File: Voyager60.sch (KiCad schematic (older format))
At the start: 231 parts, among them Q1 2N7002, SW1 6x6x5mm, U1 ATmega32U4, U2 PRTR5V0U2X, Y1 16Mhz

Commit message: Progress
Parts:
- USB1: footprint Type-C:HRO-TYPE-C-31-M-12 -> Type-C:HRO-TYPE-C-31-M-12-Assembly
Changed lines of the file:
@@
 F 0 "USB1" H 1075 9750 60  0000 C CNN
 F 1 "HRO-TYPE-C-31-M-12" V 875 9050 60  0000 C CNN
-F 2 "Type-C:HRO-TYPE-C-31-M-12" H 1275 9100 60  0001 C CNN
+F 2 "Type-C:HRO-TYPE-C-31-M-12-Assembly" H 1275 9100 60  0001 C CNN
 F 3 "" H 1275 9100 60  0001 C CNN
 	1    1275 9100

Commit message: Place components
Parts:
- removed U1: ATmega32U4, Housings_QFP:TQFP-44_10x10mm_Pitch0.8mm, symbol Voyager60-rescue:ATmega32U4
- added D44, D58, D62: SOD-123, Diodes_SMD:D_SOD-123, symbol Device:D_Small
- added K_SHIFT2: MX-1.25U, MX_Alps_Hybrid:MXOnly-1.25U, symbol MX_Alps_Hybrids:MX-1U
- added K_SHIFT3: MX-1U, MX_Alps_Hybrid:MXOnly-1U, symbol MX_Alps_Hybrids:MX-1U
- added K_SPACE3: MX-2.25U, MX_Alps_Hybrid:MXOnly-2.25U-ReversedStabilizers, symbol MX_Alps_Hybrids:MX-1U
- added K_SPACE4: MX-2.75U, MX_Alps_Hybrid:MXOnly-2.75U-ReversedStabilizers, symbol MX_Alps_Hybrids:MX-1U
- added K_SPACE5: MX-1.25U, MX_Alps_Hybrid:MXOnly-1.25U-FLIPPED, symbol MX_Alps_Hybrids:MX-1U
- added R44, R58, R62: 1k, Resistors_SMD:R_0805, symbol Device:R_Small
- added U1: ATmega32U4-MU, Housings_DFN_QFN:QFN-44-1EP_7x7mm_Pitch0.5mm, symbol MCU_Microchip_ATmega:ATmega32U4-MU
- C2, C3, C4, C5, C6, C7, C8: footprint Capacitors_SMD:C_0805 -> Capacitors_SMD:C_0603
- K_ALT2, K_RALT3: footprint MX_Alps_Hybrid:MXOnly-1.5U -> MX_Alps_Hybrid:MXOnly-1.5U-FLIPPED
- K_RALT2, K_RMENU2: footprint MX_Alps_Hybrid:MXOnly-1.25U -> MX_Alps_Hybrid:MXOnly-1.25U-FLIPPED
- K_RCTRL1, K_WIN2: footprint MX_Alps_Hybrid:MXOnly-1U -> MX_Alps_Hybrid:MXOnly-1U-FLIPPED
- K_RSHIFT1: footprint MX_Alps_Hybrid:MXOnly-2.75U -> MX_Alps_Hybrid:MXOnly-2.75U-FLIPPED
- SW1: value 6x6x5mm -> 5.2x5.2mm; footprint Molex-0548190589:PushButton_6x6mm_TH_Pretty -> Molex-0548190589:SKQG-1155865
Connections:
- net +5V: now also K_SHIFT3.3 (LED), K_SPACE3.3 (LED), K_SPACE4.3 (LED), U1.14 (VCC), U1.2 (UVCC), U1.24 (AVCC), U1.34 (VCC), U1.44 (AVCC), U1.7 (VBUS); no longer R70.1
- net COL0: now also U1.22 (PD5)
- net COL1: now also K_SHIFT3.1 (COL), U1.25 (PD4); no longer K_Z1.1 (COL)
- net COL10: now also K_.1.1 (COL), U1.37 (PF6); no longer K_/1.1 (COL)
- net COL11: now also K_/1.1 (COL), U1.38 (PF5); no longer K_RSHIFT1.1 (COL)
- net COL12: now also K_RSHIFT1.1 (COL), U1.39 (PF4)
- net COL13: now also U1.40 (PF1)
- net COL14: now also U1.41 (PF0)
- net COL2: now also K_Z1.1 (COL), U1.26 (PD6); no longer K_X1.1 (COL)
- net COL3: now also K_X1.1 (COL), K_SPACE3.1 (COL), U1.27 (PD7); no longer K_C1.1 (COL)
- net COL4: now also K_C1.1 (COL), U1.28 (PB4); no longer K_V1.1 (COL)
- net COL5: now also K_V1.1 (COL), U1.29 (PB5); no longer K_B1.1 (COL)
- net COL6: now also K_B1.1 (COL), U1.30 (PB6); no longer K_N1.1 (COL)
- net COL7: now also K_N1.1 (COL), K_SPACE4.1 (COL), U1.31 (PC6); no longer K_M1.1 (COL)
- net COL8: now also K_M1.1 (COL), U1.32 (PC7); no longer K_,1.1 (COL)
- net COL9: now also K_,1.1 (COL), U1.36 (PF7); no longer K_.1.1 (COL)
- net D+: now also U1.4 (D+)
- net D-: now also U1.3 (D-)
- net GND: now also U1.15 (GND), U1.23 (GND), U1.35 (GND), U1.43 (GND), U1.45 (GND), U1.5 (UGND)
- net LEDGND: now also R44.2, R58.2, R62.2
- net ROW0: now also U1.11 (PB3)
- net ROW1: now also U1.18 (PD0)
- net ROW2: now also U1.19 (PD1)
- net ROW3: now also D44.1 (K), U1.20 (PD2)
- net ROW4: now also D58.1 (K), D62.1 (K), U1.21 (PD3)
- net at R69.2: now also U1.12 (PB7)
- net at R70.2, SW1.2: now also U1.13 (~RESET)
- net at C8.1, Y1.3: now also U1.16 (XTAL2)
- net at C7.1, Y1.1: now also U1.17 (XTAL1)
- net at R71.2: now also U1.33 (~HWB~/PE2)
- net at C6.1: now also U1.6 (UCAP)
- net at R67.2, USB1.5 (DN2), USB1.7 (DN1): now also U2.3 (IO2); no longer U2.2 (IO1)
- net at R68.2, USB1.6 (DP1), USB1.8 (DP2): now also U2.2 (IO1); no longer U2.3 (IO2)
- new net: D44.2 (A), K_SHIFT3.2 (ROW)
- new net: K_SHIFT3.4 (LEDGND), R44.1
- new net: D58.2 (A), K_SPACE3.2 (ROW)
- new net: K_SPACE3.4 (LEDGND), R58.1
- new net: D62.2 (A), K_SPACE4.2 (ROW)
- new net: K_SPACE4.4 (LEDGND), R62.1
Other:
- moved on the sheet: C2, C3, C4, C5, C6, C7, C8, D46, D47, D48, D49, D50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

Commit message: Continue routing
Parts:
- removed D15: SOD-123, Diodes_SMD:D_SOD-123, symbol Device:D_Small
- removed K_EX1, K_RALT1, K_RMENU1, K_RWIN1, K_SRSHIFT4: MX-1U, MX_Alps_Hybrid:MXOnly-1U, symbol MX_Alps_Hybrids:MX-1U
- removed K_RCTRL1: MX-1U, MX_Alps_Hybrid:MXOnly-1U-FLIPPED, symbol MX_Alps_Hybrids:MX-1U
- removed K_SRSHIFT3: MX-1.75U, MX_Alps_Hybrid:MXOnly-1.75U, symbol MX_Alps_Hybrids:MX-1U
- removed R15: 1k, Resistors_SMD:R_0805, symbol Device:R_Small
- K_#1, K_#10, K_#2, K_#3, K_#4, K_#5, K_#6, K_#7, K_#8, K_#9, K_'1, K_,1, K_-1, K_.1, K_/1, K_;1, K_=1, K_A1, K_B1, K_C1, K_D1, K_E1, K_ESC1, K_F1, K_G1, K_H1, K_I1, K_J1, K_K1, K_L1, K_M1, K_N1, K_O1, K_P1, K_Q1, K_R1, K_RWIN3, K_S1, K_SBACK1, K_SBACK2, K_SHIFT3, K_SRSHIFT2, K_T1, K_U1, K_V1, K_W1, K_X1, K_Y1, K_Z1, K_[1, K_\2, K_]1: footprint MX_Alps_Hybrid:MXOnly-1U -> MX_Alps_Hybrid:MX-1U
- K_ALT1, K_CTRL1, K_RCTRL2, K_RWIN2, K_SHIFT2, K_WIN1: footprint MX_Alps_Hybrid:MXOnly-1.25U -> MX_Alps_Hybrid:MX-1.25U
- K_ALT2, K_CTRL2, K_RALT3: footprint MX_Alps_Hybrid:MXOnly-1.5U-FLIPPED -> MX_Alps_Hybrid:MX-1.5U-FLIPPED
- K_BACK1: footprint MX_Alps_Hybrid:MXOnly-2U -> MX_Alps_Hybrid:MX-2U
- K_CAPS1, K_SRSHIFT1: footprint MX_Alps_Hybrid:MXOnly-1.75U -> MX_Alps_Hybrid:MX-1.75U
- K_CAPS2, K_RALT2, K_RMENU2, K_SPACE5: footprint MX_Alps_Hybrid:MXOnly-1.25U-FLIPPED -> MX_Alps_Hybrid:MX-1.25U-FLIPPED
- K_ENTER1, K_SHIFT1: footprint MX_Alps_Hybrid:MXOnly-2.25U -> MX_Alps_Hybrid:MX-2.25U
- K_ENTER2: footprint MX_Alps_Hybrid:MXOnly-ISO-ROTATED-ReversedStabilizers -> MX_Alps_Hybrid:MX-ISO-ReversedStabilizers
- K_RCTRL3: footprint MX_Alps_Hybrid:MXOnly-1.5U -> MX_Alps_Hybrid:MX-1.5U-FLIPPED
- K_RSHIFT1: footprint MX_Alps_Hybrid:MXOnly-2.75U-FLIPPED -> MX_Alps_Hybrid:MX-2.75U-FLIPPED
- K_SPACE1: footprint MX_Alps_Hybrid:MXOnly-7U-ReversedStabilizers -> MX_Alps_Hybrid:MX-7U-ReversedStabilizers
- K_SPACE2: footprint MX_Alps_Hybrid:MXOnly-6.25U-ReversedStabilizers -> MX_Alps_Hybrid:MX-6.25U-ReversedStabilizers
- K_SPACE3: footprint MX_Alps_Hybrid:MXOnly-2.25U-ReversedStabilizers -> MX_Alps_Hybrid:MX-2.25U-ReversedStabilizers
- K_SPACE4: footprint MX_Alps_Hybrid:MXOnly-2.75U-ReversedStabilizers -> MX_Alps_Hybrid:MX-2.75U-ReversedStabilizers
- K_TAB1, K_\1: footprint MX_Alps_Hybrid:MXOnly-1.5U -> MX_Alps_Hybrid:MX-1.5U
- K_WIN2: footprint MX_Alps_Hybrid:MXOnly-1U-FLIPPED -> MX_Alps_Hybrid:MX-1U-FLIPPED
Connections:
- net +5V: now also K_ENTER2.3 (LED), K_RALT2.3 (LED), K_RALT3.3 (LED), K_RCTRL2.3 (LED), K_RCTRL3.3 (LED), K_RMENU2.3 (LED), K_RWIN2.3 (LED), K_RWIN3.3 (LED), K_SPACE5.3 (LED), K_SRSHIFT1.3 (LED), K_\2.3 (LED), R70.1
- net COL0: now also U1.38 (PF5); no longer U1.22 (PD5)
- net COL1: now also U1.36 (PF7); no longer U1.25 (PD4)
- net COL10: now also K_RALT2.1 (COL), U1.26 (PD6); no longer U1.37 (PF6)
- net COL11: now also K_RALT3.1 (COL), K_RWIN2.1 (COL), U1.25 (PD4); no longer U1.38 (PF5)
- net COL12: now also K_RMENU2.1 (COL), K_RWIN3.1 (COL), K_SRSHIFT1.1 (COL), U1.22 (PD5); no longer U1.39 (PF4)
- net COL13: now also K_ENTER2.1 (COL), K_RCTRL2.1 (COL), K_RCTRL3.1 (COL), K_\2.1 (COL), U1.21 (PD3); no longer U1.40 (PF1)
- net COL2: now also U1.37 (PF6); no longer U1.26 (PD6)
- net COL3: now also U1.39 (PF4); no longer K_SPACE3.1 (COL), U1.27 (PD7)
- net COL4: now also K_SPACE3.1 (COL), U1.32 (PC7); no longer U1.28 (PB4)
- net COL5: now also U1.31 (PC6); no longer K_SPACE1.1 (COL), K_SPACE2.2 (ROW), U1.29 (PB5)
- net COL6: now also K_SPACE1.1 (COL), K_SPACE2.1 (COL), K_SPACE5.2 (ROW)
- net COL7: now also U1.29 (PB5); no longer K_SPACE4.1 (COL), U1.31 (PC6)
- net COL8: now also K_SPACE4.1 (COL), U1.28 (PB4); no longer U1.32 (PC7)
- net COL9: now also U1.27 (PD7); no longer U1.36 (PF7)
- net ROW0: now also U1.9 (PB1); no longer U1.11 (PB3)
- net ROW1: now also U1.10 (PB2); no longer U1.18 (PD0)
- net ROW2: now also U1.11 (PB3); no longer U1.19 (PD1)
- net ROW3: now also U1.19 (PD1); no longer U1.20 (PD2)
- net ROW4: now also U1.20 (PD2); no longer U1.21 (PD3)
- net at D29.2 (A), K_\1.2 (ROW): now also K_\2.2 (ROW)
- net at K_\1.4 (LEDGND), R29.1: now also K_\2.4 (LEDGND)
- net at D43.2 (A), K_ENTER1.2 (ROW): now also K_ENTER2.2 (ROW)
- net at K_ENTER1.4 (LEDGND), R43.1: now also K_ENTER2.4 (LEDGND)
- net at D56.2 (A), K_RSHIFT1.2 (ROW): now also K_SRSHIFT1.2 (ROW)
- net at K_RSHIFT1.4 (LEDGND), R56.1: now also K_SRSHIFT1.4 (LEDGND)
- net at D61.2 (A), K_SPACE1.2 (ROW): now also K_SPACE2.2 (ROW), K_SPACE5.1 (COL); no longer K_SPACE2.1 (COL)
- net at K_SPACE1.4 (LEDGND), K_SPACE2.4 (LEDGND), R61.1: now also K_SPACE5.4 (LEDGND)
- net at D63.2 (A): now also K_RALT2.2 (ROW)
- net at R63.1: now also K_RALT2.4 (LEDGND)
- net at D64.2 (A): now also K_RALT3.2 (ROW), K_RWIN2.2 (ROW)
- net at R64.1: now also K_RALT3.4 (LEDGND), K_RWIN2.4 (LEDGND)
- net at D65.2 (A): now also K_RCTRL2.2 (ROW), K_RCTRL3.2 (ROW)
- net at R65.1: now also K_RCTRL2.4 (LEDGND), K_RCTRL3.4 (LEDGND)
- net at D30.2 (A): now also K_RMENU2.2 (ROW), K_RWIN3.2 (ROW)
- net at R30.1: now also K_RMENU2.4 (LEDGND), K_RWIN3.4 (LEDGND)
- net COL14: no longer names the net of U1.41 (PF0)
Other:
- moved on the sheet: D58, D61, D62, K_RALT2, K_RALT3, K_RCTRL2, K_RCTRL3, K_RMENU2, K_RWIN2, K_RWIN3, K_SPACE1, K_SPACE2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

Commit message: Continue routing
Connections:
- net +5V: now also K_SHIFT2.3 (LED)
- net COL0: now also K_SHIFT2.1 (COL)
- net COL1: now also K_WIN2.1 (COL); no longer K_WIN2.2 (ROW)
- net at D45.2 (A), K_SHIFT1.2 (ROW): now also K_SHIFT2.2 (ROW)
- net at K_SHIFT1.4 (LEDGND), R45.1: now also K_SHIFT2.4 (LEDGND)
- net at D60.2 (A), K_WIN1.2 (ROW): now also K_WIN2.2 (ROW); no longer K_WIN2.1 (COL)
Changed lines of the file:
@@
 	1325 4075 1325 4700
-Wire Wire Line
-	2075 4550 2075 4375
-Wire Wire Line
-	2075 4375 1875 4375
-Wire Wire Line
-	1875 4375 1875 4125
-Wire Wire Line
-	1875 4750 1700 4750
-Wire Wire Line
-	1700 4750 1700 3925
-Wire Wire Line
-	1700 3925 2075 3925
 Wire Wire Line
 	2125 4600 2025 4600
@@
 	9475 3150 9475 3475
 Connection ~ 8475 3475
+Wire Wire Line
+	2075 3925 2075 4550
+Connection ~ 2075 3925
+Wire Wire Line
+	1875 4750 1875 4125
+Connection ~ 1875 4125
+Wire Wire Line
+	1475 3275 925  3275
+Wire Wire Line
+	725  3475 1200 3475
+Connection ~ 1200 3475
+Wire Wire Line
+	1325 3425 775  3425
+Connection ~ 1325 3425
+Wire Wire Line
+	875  3325 1425 3325
+Connection ~ 1425 3325
 $EndSCHEMATC

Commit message: Progress
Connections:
- net COL0: now also U1.39 (PF4); no longer U1.38 (PF5)
- net COL2: now also U1.38 (PF5); no longer U1.37 (PF6)
- net COL3: now also U1.37 (PF6); no longer U1.39 (PF4)
- net ROW3: now also U1.41 (PF0); no longer U1.19 (PD1)
- net ROW4: now also U1.40 (PF1); no longer U1.20 (PD2)
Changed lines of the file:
@@
 Text GLabel 8750 7300 2    60   Input ~ 0
 COL4
-Text GLabel 8750 8900 2    60   Input ~ 0
+Text GLabel 8750 9100 2    60   Input ~ 0
 COL3
-Text GLabel 8750 9100 2    60   Input ~ 0
+Text GLabel 8750 9000 2    60   Input ~ 0
 COL2
 Text GLabel 8750 9200 2    60   Input ~ 0
 COL1
-Text GLabel 8750 9000 2    60   Input ~ 0
+Text GLabel 8750 8900 2    60   Input ~ 0
 COL0
-Text GLabel 8750 7700 2    60   Input ~ 0
+Text GLabel 8750 8800 2    60   Input ~ 0
 ROW4
-Text GLabel 8750 7600 2    60   Input ~ 0
+Text GLabel 8750 8700 2    60   Input ~ 0
 ROW3
 Text GLabel 8750 6600 2    60   Input ~ 0

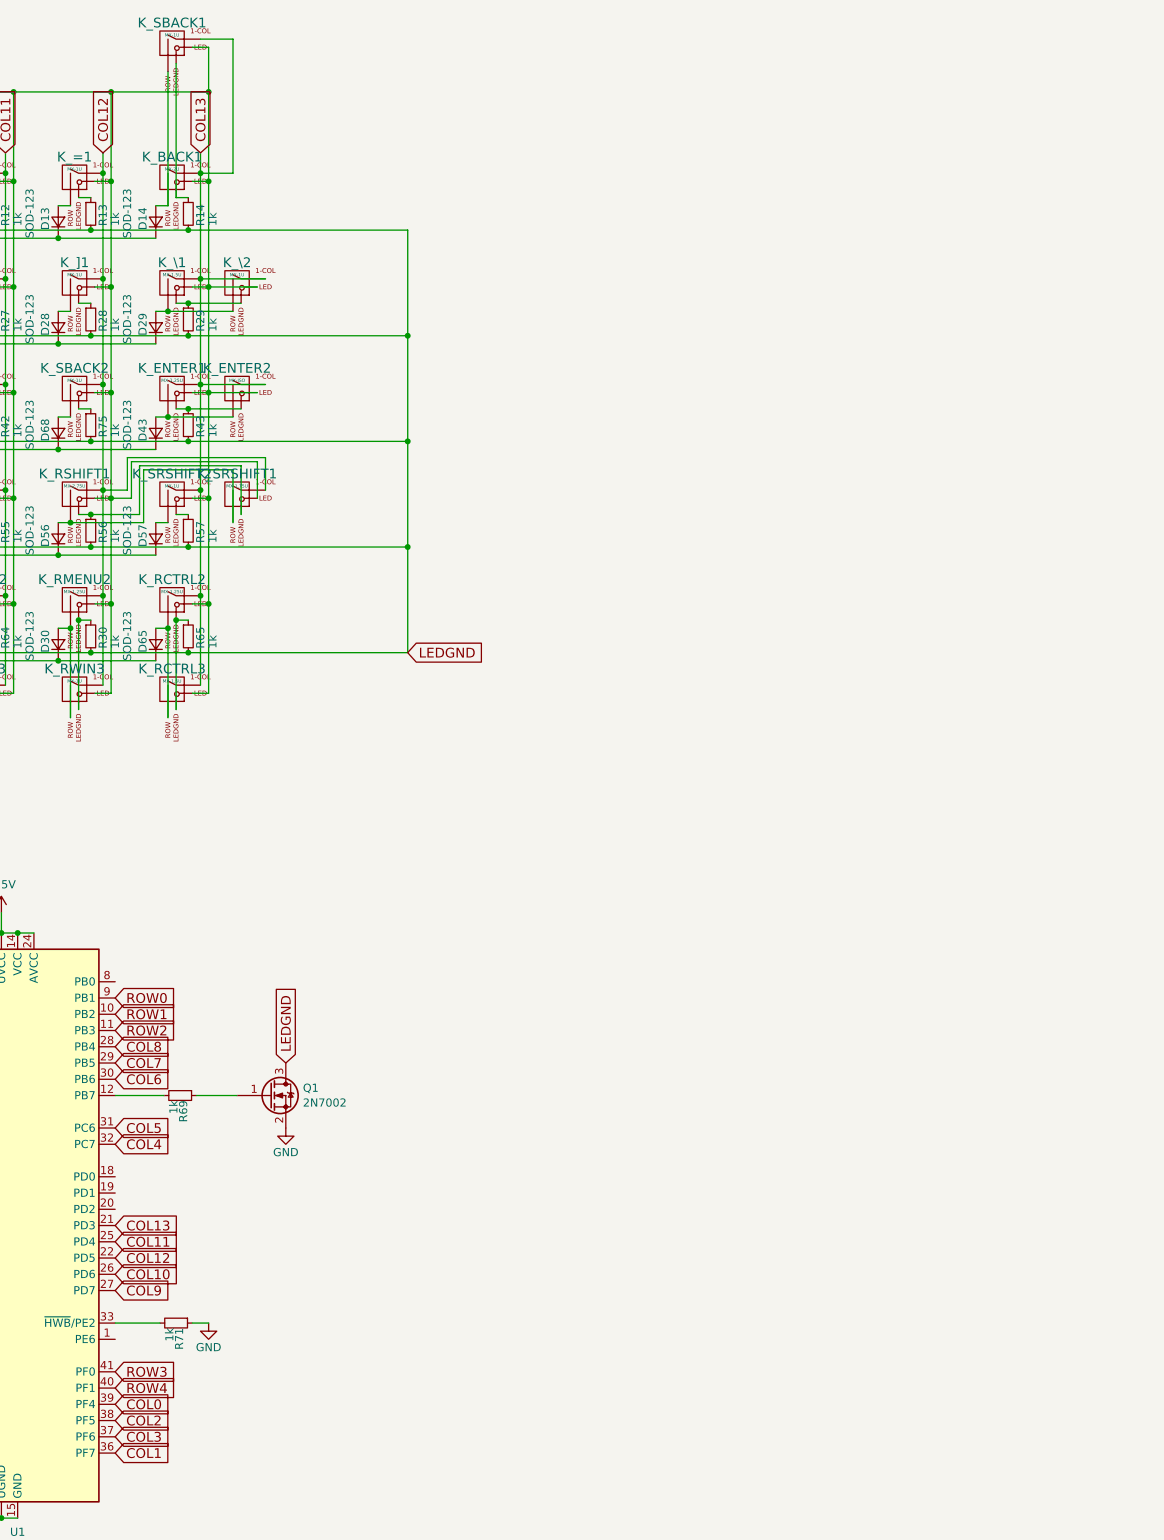
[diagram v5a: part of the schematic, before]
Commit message: Route RGBs
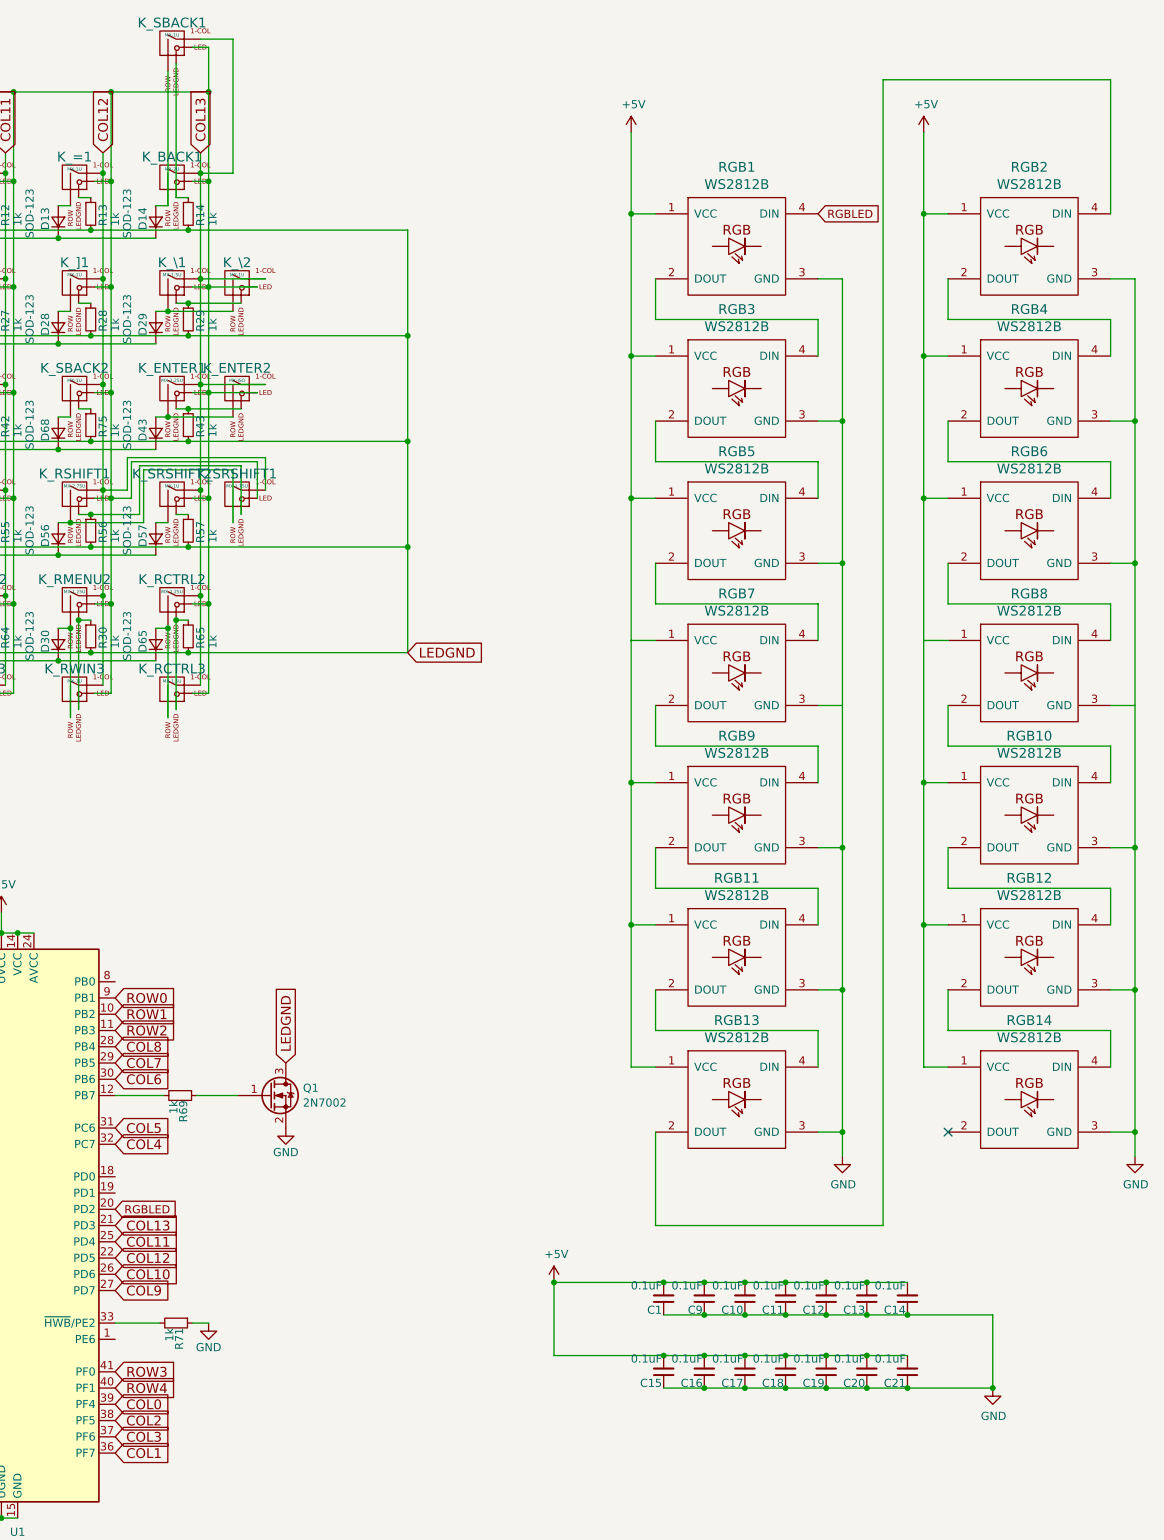
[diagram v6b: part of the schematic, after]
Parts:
- added C1, C10, C11, C12, C13, C14, C15, C16, C17, C18, C19, C20, C21, C9: 0.1uF, Capacitors_SMD:C_0603, symbol Device:C_Small
- added RGB1, RGB10, RGB11, RGB12, RGB13, RGB14, RGB2, RGB3, RGB4, RGB5, RGB6, RGB7, RGB8, RGB9: WS2812B, WS2812B:WS2812B, symbol ws2812b:WS2812B
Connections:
- net +5V: now also C1.2, C10.2, C11.2, C12.2, C13.2, C14.2, C15.2, C16.2, C17.2, C18.2, C19.2, C20.2, C21.2, C9.2, RGB1.1 (VCC), RGB10.1 (VCC), RGB11.1 (VCC), RGB12.1 (VCC), RGB13.1 (VCC), RGB14.1 (VCC), RGB2.1 (VCC), RGB3.1 (VCC), RGB4.1 (VCC), RGB5.1 (VCC), RGB6.1 (VCC), RGB7.1 (VCC), RGB8.1 (VCC), RGB9.1 (VCC)
- net GND: now also C1.1, C10.1, C11.1, C12.1, C13.1, C14.1, C15.1, C16.1, C17.1, C18.1, C19.1, C20.1, C21.1, C9.1, RGB1.3 (GND), RGB10.3 (GND), RGB11.3 (GND), RGB12.3 (GND), RGB13.3 (GND), RGB14.3 (GND), RGB2.3 (GND), RGB3.3 (GND), RGB4.3 (GND), RGB5.3 (GND), RGB6.3 (GND), RGB7.3 (GND), RGB8.3 (GND), RGB9.3 (GND)
- net RGBLED: now reaches U1.20 (PD2)
- net RGBLED: now also RGB1.4 (DIN)
- new net: RGB1.2 (DOUT), RGB3.4 (DIN)
- new net: RGB3.2 (DOUT), RGB5.4 (DIN)
- new net: RGB5.2 (DOUT), RGB7.4 (DIN)
- new net: RGB7.2 (DOUT), RGB9.4 (DIN)
- new net: RGB11.4 (DIN), RGB9.2 (DOUT)
- new net: RGB11.2 (DOUT), RGB13.4 (DIN)
- new net: RGB13.2 (DOUT), RGB2.4 (DIN)
- new net: RGB2.2 (DOUT), RGB4.4 (DIN)
- new net: RGB4.2 (DOUT), RGB6.4 (DIN)
- new net: RGB6.2 (DOUT), RGB8.4 (DIN)
- new net: RGB10.4 (DIN), RGB8.2 (DOUT)
- new net: RGB10.2 (DOUT), RGB12.4 (DIN)
- new net: RGB12.2 (DOUT), RGB14.4 (DIN)
- no-connect marks 1 -> 2

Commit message: Make alps variant
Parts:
- removed Q1: 2N7002, TO_SOT_Packages_SMD:SOT-23, symbol Transistor_FET:2N7002
- removed R1, R10, R11, R12, R13, R14, R16, R17, R18, R19, R2, R20, R21, R22, R23, R24, R25, R26, R27, R28, R29, R3, R30, R31, R32, R33, R34, R35, R36, R37, R38, R39, R4, R40, R41, R42, R43, R44, R45, R46, R47, R48, R49, R5, R50, R51, R52, R53, R54, R55, R56, R57, R58, R59, R6, R60, R61, R62, R63, R64, R65, R69, R7, R72, R75, R8, R9: 1k, Resistors_SMD:R_0805, symbol Device:R_Small
- added K_ALT3, K_CAPS3, K_RALT1: MX-1.5U, MX_Alps_Hybrid:ALPS-1.5U, symbol MX_Alps_Hybrids:MX-1U
- added K_ENTER3, K_ENTER4, K_ESC2: MX-1U, MX_Alps_Hybrid:ALPS-1U, symbol MX_Alps_Hybrids:MX-1U
- added K_RWIN1, K_WIN3: MX-1.25U, MX_Alps_Hybrid:ALPS-1.25U, symbol MX_Alps_Hybrids:MX-1U
- K_#1, K_#10, K_#2, K_#3, K_#4, K_#5, K_#6, K_#7, K_#8, K_#9, K_'1, K_,1, K_-1, K_.1, K_/1, K_;1, K_=1, K_A1, K_B1, K_C1, K_D1, K_E1, K_ESC1, K_F1, K_G1, K_H1, K_I1, K_J1, K_K1, K_L1, K_M1, K_N1, K_O1, K_P1, K_Q1, K_R1, K_RWIN3, K_S1, K_SBACK1, K_SBACK2, K_SHIFT3, K_SRSHIFT2, K_T1, K_U1, K_V1, K_W1, K_X1, K_Y1, K_Z1, K_[1, K_\2, K_]1: footprint MX_Alps_Hybrid:MX-1U -> MX_Alps_Hybrid:ALPS-1U
- K_ALT1, K_CTRL1, K_RCTRL2, K_RWIN2, K_SHIFT2, K_WIN1: footprint MX_Alps_Hybrid:MX-1.25U -> MX_Alps_Hybrid:ALPS-1.25U
- K_ALT2, K_CTRL2, K_RALT3, K_RCTRL3: footprint MX_Alps_Hybrid:MX-1.5U-FLIPPED -> MX_Alps_Hybrid:ALPS-1.5U
- K_BACK1: footprint MX_Alps_Hybrid:MX-2U -> MX_Alps_Hybrid:ALPS-2U
- K_CAPS1, K_SRSHIFT1: footprint MX_Alps_Hybrid:MX-1.75U -> MX_Alps_Hybrid:ALPS-1.75U
- K_CAPS2, K_RALT2, K_RMENU2, K_SPACE5: footprint MX_Alps_Hybrid:MX-1.25U-FLIPPED -> MX_Alps_Hybrid:ALPS-1.25U
- K_ENTER1, K_SHIFT1: footprint MX_Alps_Hybrid:MX-2.25U -> MX_Alps_Hybrid:ALPS-2.25U
- K_ENTER2: value MX-ISO -> MX-1U; footprint MX_Alps_Hybrid:MX-ISO-ReversedStabilizers -> MX_Alps_Hybrid:ALPS-1U
- K_RSHIFT1: footprint MX_Alps_Hybrid:MX-2.75U-FLIPPED -> MX_Alps_Hybrid:ALPS-2.75U
- K_SPACE1: footprint MX_Alps_Hybrid:MX-7U-ReversedStabilizers -> MX_Alps_Hybrid:ALPS-7U
- K_SPACE2: footprint MX_Alps_Hybrid:MX-6.25U-ReversedStabilizers -> MX_Alps_Hybrid:ALPS-6.25U
- K_SPACE3: footprint MX_Alps_Hybrid:MX-2.25U-ReversedStabilizers -> MX_Alps_Hybrid:ALPS-2.25U
- K_SPACE4: footprint MX_Alps_Hybrid:MX-2.75U-ReversedStabilizers -> MX_Alps_Hybrid:ALPS-2.75U
- K_TAB1, K_\1: footprint MX_Alps_Hybrid:MX-1.5U -> MX_Alps_Hybrid:ALPS-1.5U
- K_WIN2: footprint MX_Alps_Hybrid:MX-1U-FLIPPED -> MX_Alps_Hybrid:ALPS-1U
- U1: symbol MCU_Microchip_ATmega:ATmega32U4-MU -> Voyager60-rescue:ATmega32U4-MU-MCU_Microchip_ATmega
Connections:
- net labels removed: LEDGND
- wire segments 788 -> 646
